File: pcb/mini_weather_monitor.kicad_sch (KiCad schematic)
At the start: 6 parts, among them U1 module_mpu6050, U2 4.0inch_SPI_MSP4021, U2_BME280 module_bme280, U3 neo6mv2, U3_BH1750 module_bh1750

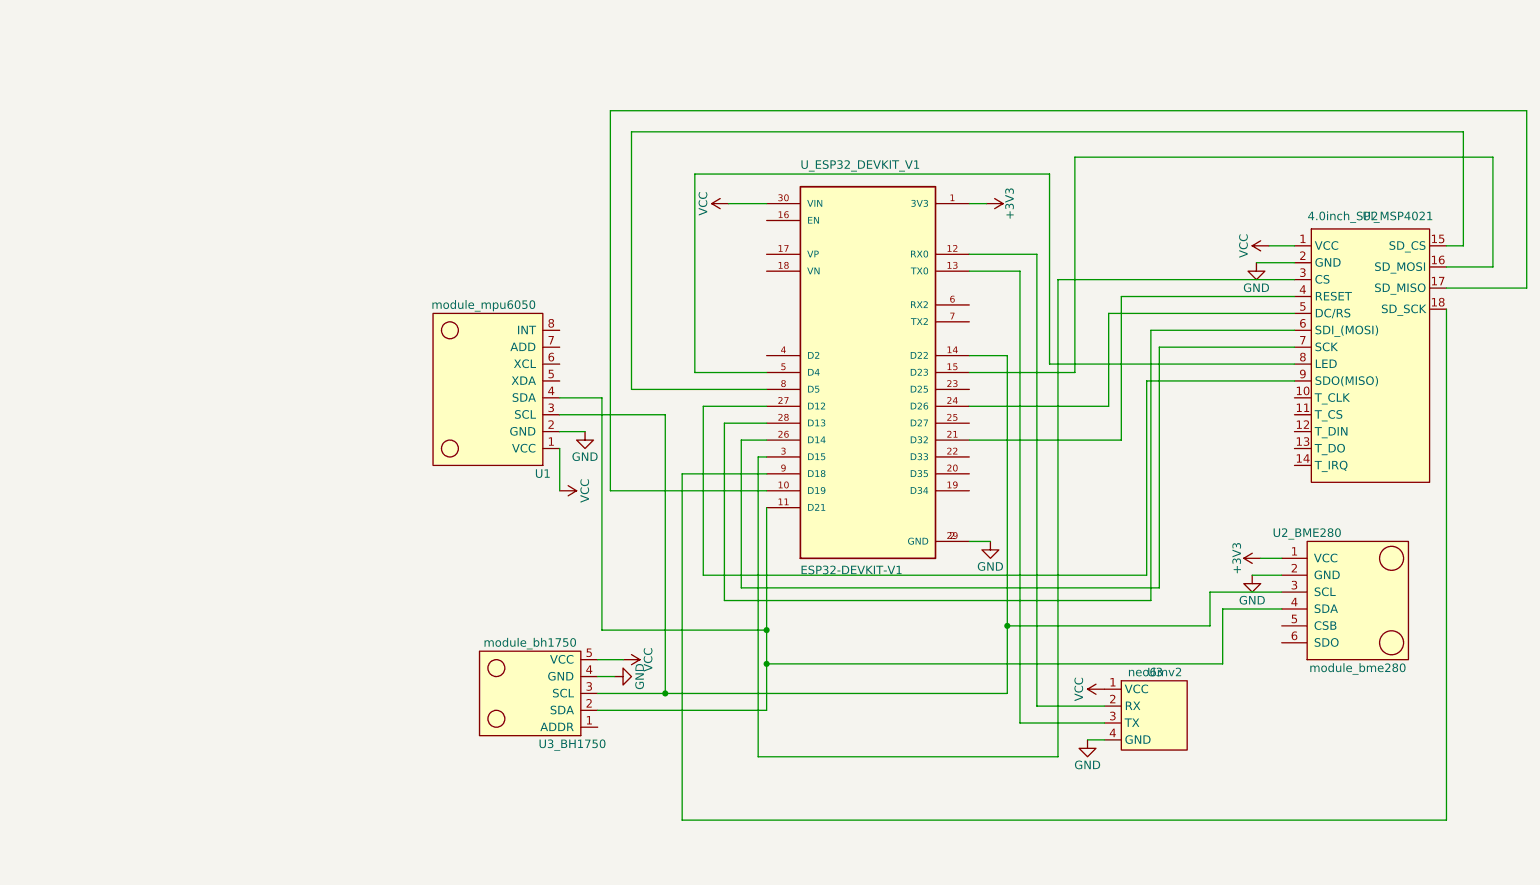
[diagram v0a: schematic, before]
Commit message: wip, with MPU6050, but will switch to SW520D
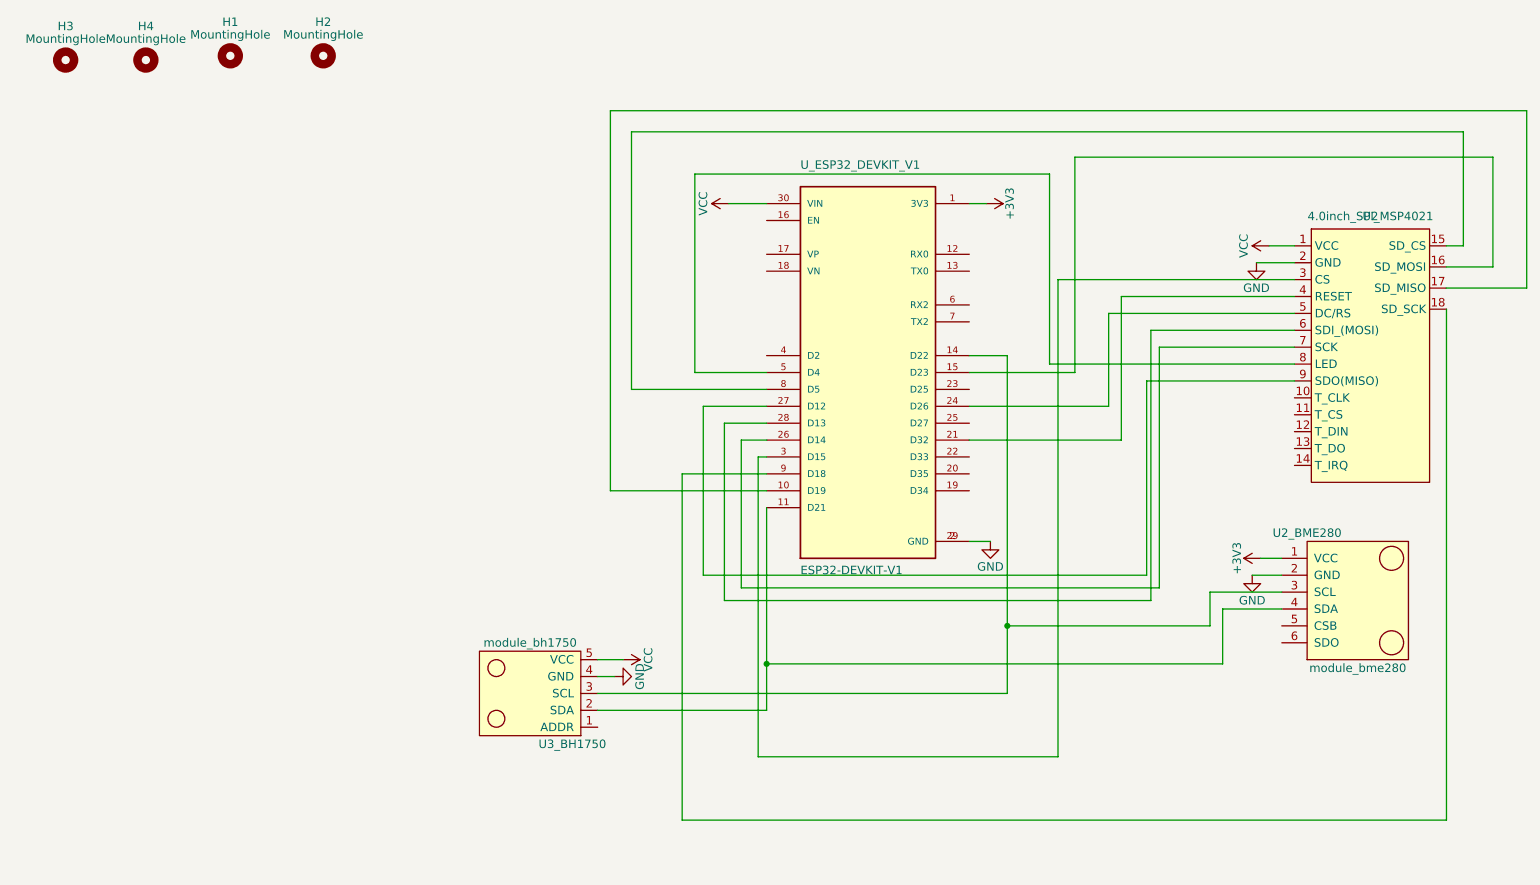
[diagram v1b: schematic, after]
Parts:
- removed U1: module_mpu6050, usini_sensors:module_mpu6050, symbol usini_sensors:module_mpu6050
- removed U3: neo6mv2, gps:GY-NEO6MV2, symbol gps:neo6mv2
- added H1, H2, H3, H4: MountingHole, MountingHole:MountingHole_2.2mm_M2, symbol Mechanical:MountingHole

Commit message: fixing orientation with new tilt sensor and adding libraries to repo
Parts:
- added J1: SW-520D, symbol Connector_Generic:Conn_01x03
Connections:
- net GND: now also J1.3 (Pin_3)
- net VCC: now also J1.2 (Pin_2)
- net at U_ESP32_DEVKIT_V1.4 (D2): now also J1.1 (Pin_1)
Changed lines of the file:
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@@
+    (stroke (width 0) (type default) (color 0 0 0 0))
+  )
+  (wire (pts (xy 78.105 86.995) (xy 98.425 86.995))
     (stroke (width 0) (type default) (color 0 0 0 0))
   )
@@
     (stroke (width 0) (type default) (color 0 0 0 0))
   )
+  (wire (pts (xy 98.425 86.995) (xy 98.425 69.215))
+    (stroke (width 0) (type default) (color 0 0 0 0))
+  )
   (wire (pts (xy 169.545 57.785) (xy 169.545 129.54))
     (stroke (width 0) (type default) (color 0 0 0 0))
@@
   )
   (wire (pts (xy 198.755 102.235) (xy 203.2 102.235))
+    (stroke (width 0) (type default) (color 0 0 0 0))
+  )
+  (wire (pts (xy 98.425 69.215) (xy 125.73 69.215))
     (stroke (width 0) (type default) (color 0 0 0 0))
   )
@@
     (pin "5")
     (pin "6")
+  )
+  (symbol (lib_id "power:VCC") (at 78.105 84.455 270) (unit 1)
+    (in_bom yes) (on_board yes)
+    (property "Reference" "#PWR?" (id 0) (at 74.295 84.455 0)
+      (effects (font (size 1.27 1.27)) hide)
+    )
+    (property "Value" "VCC" (id 1) (at 81.915 84.455 0))
+    (property "Footprint" "" (id 2) (at 78.105 84.455 0)
+      (effects (font (size 1.27 1.27)) hide)
+    )
+    (property "Datasheet" "" (id 3) (at 78.105 84.455 0)
+      (effects (font (size 1.27 1.27)) hide)
+    )
+    (pin "1")
   )
   (symbol (lib_id "Mechanical:MountingHole") (at 45.085 24.13 0) (unit 1)
@@
     (pin "1")
   )
+  (symbol (lib_id "power:GND") (at 78.105 81.915 90) (unit 1)
+    (in_bom yes) (on_board yes)
+    (property "Reference" "#PWR?" (id 0) (at 84.455 81.915 0)
+      (effects (font (size 1.27 1.27)) hide)
+    )
+    (property "Value" "GND" (id 1) (at 81.915 81.915 0))
+    (property "Footprint" "" (id 2) (at 78.105 81.915 0)
+      (effects (font (size 1.27 1.27)) hide)
+    )
+    (property "Datasheet" "" (id 3) (at 78.105 81.915 0)
+      (effects (font (size 1.27 1.27)) hide)
+    )
+    (pin "1")
+  )
   (symbol (lib_id "usini_sensors:module_bh1750") (at 100.33 117.475 180) (unit 1)
     (in_bom yes) (on_board yes)
@@
     (pin "4")
     (pin "5")
+  )
+  (symbol (lib_id "Connector_Generic:Conn_01x03") (at 73.025 84.455 180) (unit 1)
+    (in_bom yes) (on_board yes)
+    (property "Reference" "J1" (id 0) (at 73.025 89.535 0))
+    (property "Value" "SW-520D" (id 1) (at 73.025 79.375 0))
+    (property "Footprint" "" (id 2) (at 73.025 84.455 0)
+      (effects (font (size 1.27 1.27)) hide)
+    )
+    (property "Datasheet" "~" (id 3) (at 73.025 84.455 0)
+      (effects (font (size 1.27 1.27)) hide)
+    )
+    (pin "1")
+    (pin "2")
+    (pin "3")
   )
   (symbol (lib_id "power:GND") (at 199.39 55.245 0) (unit 1)
@@
       (reference "#PWR0111") (unit 1) (value "VCC") (footprint "")
     )
+    (path "/1e01b4d9-a989-409c-94fd-57d5171ccf78"
+      (reference "#PWR?") (unit 1) (value "VCC") (footprint "")
+    )
+    (path "/47b6694c-c477-4176-af38-50c331ec0ae7"
+      (reference "#PWR?") (unit 1) (value "GND") (footprint "")
+    )
     (path "/1ed3e5bb-623c-4717-afd1-5e05574edbe0"
       (reference "H1") (unit 1) (value "MountingHole") (footprint "MountingHole:MountingHole_2.2mm_M2")
@@
       (reference "H4") (unit 1) (value "MountingHole") (footprint "MountingHole:MountingHole_2.2mm_M2")
     )
+    (path "/614a403a-474a-4306-b606-97f15c564ef8"
+      (reference "J1") (unit 1) (value "SW-520D") (footprint "")
+    )
     (path "/2aa21e55-25c6-4cf4-bd8a-94f164963f6d"

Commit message: fixxing footprint and pad
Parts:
- added U1: PowerSupplyMB102_v13, power_supplies:POWERSUPPLYMB102, symbol power_supplyies:PowerSupplyMB102_v13
- J1: footprint (none) -> Connector_PinHeader_2.54mm:PinHeader_1x03_P2.54mm_Horizontal
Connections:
- net +3V3: now also U1.5 (VCC2), U1.7 (VCC2)
- net GND: now also U1.2 (GND), U1.6 (GND), U1.8 (GND)
- net VCC: now also U1.1 (VCC1), U1.3 (VCC1)
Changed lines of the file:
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@@
   (symbol (lib_id "power:VCC") (at 78.105 84.455 270) (unit 1)
     (in_bom yes) (on_board yes)
-    (property "Reference" "#PWR?" (id 0) (at 74.295 84.455 0)
+    (property "Reference" "#PWR0102" (id 0) (at 74.295 84.455 0)
       (effects (font (size 1.27 1.27)) hide)
     )
@@
     )
     (property "Datasheet" "" (id 3) (at 159.385 97.155 0)
+      (effects (font (size 1.27 1.27)) hide)
+    )
+    (pin "1")
+  )
+  (symbol (lib_id "power:VCC") (at 82.55 38.1 270) (unit 1)
+    (in_bom yes) (on_board yes)
+    (property "Reference" "#PWR0114" (id 0) (at 78.74 38.1 0)
+      (effects (font (size 1.27 1.27)) hide)
+    )
+    (property "Value" "VCC" (id 1) (at 86.36 38.1 0))
+    (property "Footprint" "" (id 2) (at 82.55 38.1 0)
+      (effects (font (size 1.27 1.27)) hide)
+    )
+    (property "Datasheet" "" (id 3) (at 82.55 38.1 0)
       (effects (font (size 1.27 1.27)) hide)
     )
@@
   (symbol (lib_id "power:GND") (at 78.105 81.915 90) (unit 1)
     (in_bom yes) (on_board yes)
-    (property "Reference" "#PWR?" (id 0) (at 84.455 81.915 0)
+    (property "Reference" "#PWR0105" (id 0) (at 84.455 81.915 0)
       (effects (font (size 1.27 1.27)) hide)
     )
@@
     )
     (property "Datasheet" "" (id 3) (at 78.105 81.915 0)
+      (effects (font (size 1.27 1.27)) hide)
+    )
+    (pin "1")
+  )
+  (symbol (lib_id "power:+3V3") (at 21.59 38.1 90) (unit 1)
+    (in_bom yes) (on_board yes)
+    (property "Reference" "#PWR0112" (id 0) (at 25.4 38.1 0)
+      (effects (font (size 1.27 1.27)) hide)
+    )
+    (property "Value" "+3V3" (id 1) (at 18.034 38.1 0))
+    (property "Footprint" "" (id 2) (at 21.59 38.1 0)
+      (effects (font (size 1.27 1.27)) hide)
+    )
+    (property "Datasheet" "" (id 3) (at 21.59 38.1 0)
       (effects (font (size 1.27 1.27)) hide)
     )
@@
     (property "Reference" "J1" (id 0) (at 73.025 89.535 0))
     (property "Value" "SW-520D" (id 1) (at 73.025 79.375 0))
-    (property "Footprint" "" (id 2) (at 73.025 84.455 0)
+    (property "Footprint" "Connector_PinHeader_2.54mm:PinHeader_1x03_P2.54mm_Horizontal" (id 2) (at 73.025 84.455 0)
       (effects (font (size 1.27 1.27)) hide)
     )
@@
     )
     (property "Datasheet" "" (id 3) (at 199.39 55.245 0)
+      (effects (font (size 1.27 1.27)) hide)
+    )
+    (pin "1")
+  )
+  (symbol (lib_id "power:GND") (at 82.55 42.418 0) (unit 1)
+    (in_bom yes) (on_board yes)
+    (property "Reference" "#PWR0117" (id 0) (at 82.55 48.768 0)
+      (effects (font (size 1.27 1.27)) hide)
+    )
+    (property "Value" "GND" (id 1) (at 82.55 46.228 0))
+    (property "Footprint" "" (id 2) (at 82.55 42.418 0)
+      (effects (font (size 1.27 1.27)) hide)
+    )
+    (property "Datasheet" "" (id 3) (at 82.55 42.418 0)
       (effects (font (size 1.27 1.27)) hide)
     )
@@
     )
     (property "Datasheet" "" (id 3) (at 201.295 52.705 0)
+      (effects (font (size 1.27 1.27)) hide)
+    )
+    (pin "1")
+  )
+  (symbol (lib_id "power:GND") (at 82.55 59.055 0) (unit 1)
+    (in_bom yes) (on_board yes)
+    (property "Reference" "#PWR0119" (id 0) (at 82.55 65.405 0)
+      (effects (font (size 1.27 1.27)) hide)
+    )
+    (property "Value" "GND" (id 1) (at 82.55 62.865 0))
+    (property "Footprint" "" (id 2) (at 82.55 59.055 0)
+      (effects (font (size 1.27 1.27)) hide)
+    )
+    (property "Datasheet" "" (id 3) (at 82.55 59.055 0)
       (effects (font (size 1.27 1.27)) hide)
     )
@@
     (pin "9")
   )
+  (symbol (lib_id "power:GND") (at 21.59 58.674 0) (unit 1)
+    (in_bom yes) (on_board yes)
+    (property "Reference" "#PWR0116" (id 0) (at 21.59 65.024 0)
+      (effects (font (size 1.27 1.27)) hide)
+    )
+    (property "Value" "GND" (id 1) (at 21.59 62.484 0))
+    (property "Footprint" "" (id 2) (at 21.59 58.674 0)
+      (effects (font (size 1.27 1.27)) hide)
+    )
+    (property "Datasheet" "" (id 3) (at 21.59 58.674 0)
+      (effects (font (size 1.27 1.27)) hide)
+    )
+    (pin "1")
+  )
   (symbol (lib_id "power:+3V3") (at 200.025 99.695 90) (unit 1)
     (in_bom yes) (on_board yes)
@@
     )
   )
+  (symbol (lib_id "power_supplyies:PowerSupplyMB102_v13") (at 52.07 48.26 0) (unit 1)
+    (in_bom yes) (on_board yes)
+    (property "Reference" "U1" (id 0) (at 52.07 46.99 0))
+    (property "Value" "PowerSupplyMB102_v13" (id 1) (at 52.07 49.53 0))
+    (property "Footprint" "power_supplies:POWERSUPPLYMB102" (id 2) (at 52.07 48.26 0)
+      (effects (font (size 1.27 1.27)) hide)
+    )
+    (property "Datasheet" "" (id 3) (at 52.07 48.26 0)
+      (effects (font (size 1.27 1.27)) hide)
+    )
+    (pin "1")
+    (pin "2")
+    (pin "3")
+    (pin "4")
+    (pin "5")
+    (pin "6")
+    (pin "7")
+    (pin "8")
+  )
+  (symbol (lib_id "power:VCC") (at 82.55 54.61 270) (unit 1)
+    (in_bom yes) (on_board yes)
+    (property "Reference" "#PWR0118" (id 0) (at 78.74 54.61 0)
+      (effects (font (size 1.27 1.27)) hide)
+    )
+    (property "Value" "VCC" (id 1) (at 86.36 54.61 0))
+    (property "Footprint" "" (id 2) (at 82.55 54.61 0)
+      (effects (font (size 1.27 1.27)) hide)
+    )
+    (property "Datasheet" "" (id 3) (at 82.55 54.61 0)
+      (effects (font (size 1.27 1.27)) hide)
+    )
+    (pin "1")
+  )
   (symbol (lib_id "power:VCC") (at 104.14 114.935 270) (unit 1)
     (in_bom yes) (on_board yes)
@@
     )
   )
+  (symbol (lib_id "power:GND") (at 21.59 42.418 0) (unit 1)
+    (in_bom yes) (on_board yes)
+    (property "Reference" "#PWR0115" (id 0) (at 21.59 48.768 0)
+      (effects (font (size 1.27 1.27)) hide)
+    )
+    (property "Value" "GND" (id 1) (at 21.59 46.228 0))
+    (property "Footprint" "" (id 2) (at 21.59 42.418 0)
+      (effects (font (size 1.27 1.27)) hide)
+    )
+    (property "Datasheet" "" (id 3) (at 21.59 42.418 0)
+      (effects (font (size 1.27 1.27)) hide)
+    )
+    (pin "1")
+  )
   (symbol (lib_id "power:VCC") (at 120.015 46.355 90) (unit 1)
     (in_bom yes) (on_board yes)
@@
     )
     (property "Datasheet" "" (id 3) (at 120.015 46.355 0)
+      (effects (font (size 1.27 1.27)) hide)
+    )
+    (pin "1")
+  )
+  (symbol (lib_id "power:+3V3") (at 21.59 54.356 90) (unit 1)
+    (in_bom yes) (on_board yes)
+    (property "Reference" "#PWR0113" (id 0) (at 25.4 54.356 0)
+      (effects (font (size 1.27 1.27)) hide)
+    )
+    (property "Value" "+3V3" (id 1) (at 18.034 54.356 0))
+    (property "Footprint" "" (id 2) (at 21.59 54.356 0)
+      (effects (font (size 1.27 1.27)) hide)
+    )
+    (property "Datasheet" "" (id 3) (at 21.59 54.356 0)
       (effects (font (size 1.27 1.27)) hide)
     )
@@
       (reference "#PWR0101") (unit 1) (value "GND") (footprint "")
     )
+    (path "/1e01b4d9-a989-409c-94fd-57d5171ccf78"
+      (reference "#PWR0102") (unit 1) (value "VCC") (footprint "")
+    )
     (path "/1f388e68-7a67-4769-ab0f-bc8bbfd33e19"
       (reference "#PWR0103") (unit 1) (value "GND") (footprint "")
@@
       (reference "#PWR0104") (unit 1) (value "GND") (footprint "")
     )
+    (path "/47b6694c-c477-4176-af38-50c331ec0ae7"
+      (reference "#PWR0105") (unit 1) (value "GND") (footprint "")
+    )
     (path "/3db7a179-de3e-48c9-994f-6f4a8f7a50e2"
       (reference "#PWR0106") (unit 1) (value "+3V3") (footprint "")
@@
       (reference "#PWR0111") (unit 1) (value "VCC") (footprint "")
     )
-    (path "/1e01b4d9-a989-409c-94fd-57d5171ccf78"
-      (reference "#PWR?") (unit 1) (value "VCC") (footprint "")
-    )
-    (path "/47b6694c-c477-4176-af38-50c331ec0ae7"
-      (reference "#PWR?") (unit 1) (value "GND") (footprint "")
+    (path "/4f3560be-1f70-4fa1-aade-f6678352e498"
+      (reference "#PWR0112") (unit 1) (value "+3V3") (footprint "")
+    )
+    (path "/fa6e591d-2fb3-41d0-89e1-7ff8a72bbcbf"
+      (reference "#PWR0113") (unit 1) (value "+3V3") (footprint "")
+    )
+    (path "/26ee0bb2-ad6d-413d-98eb-7ee5ee45f359"
+      (reference "#PWR0114") (unit 1) (value "VCC") (footprint "")
+    )
+    (path "/f2ef21bc-1542-49c2-acb2-773f89f4450e"
+      (reference "#PWR0115") (unit 1) (value "GND") (footprint "")
+    )
+    (path "/b5d4c2a9-513a-4b02-8fe0-a6fb67e94f7f"
+      (reference "#PWR0116") (unit 1) (value "GND") (footprint "")
+    )
+    (path "/6ee1587a-a7da-4728-ab8c-6e3d2518a1e3"
+      (reference "#PWR0117") (unit 1) (value "GND") (footprint "")
+    )
+    (path "/dd7408e6-f877-4a6b-998a-3f52cade8029"
+      (reference "#PWR0118") (unit 1) (value "VCC") (footprint "")
+    )
+    (path "/a77e472e-db3b-404f-8e27-ca00131b5c5a"
+      (reference "#PWR0119") (unit 1) (value "GND") (footprint "")
     )
     (path "/1ed3e5bb-623c-4717-afd1-5e05574edbe0"
@@
     )
     (path "/614a403a-474a-4306-b606-97f15c564ef8"
-      (reference "J1") (unit 1) (value "SW-520D") (footprint "")
+      (reference "J1") (unit 1) (value "SW-520D") (footprint "Connector_PinHeader_2.54mm:PinHeader_1x03_P2.54mm_Horizontal")
+    )
+    (path "/d768292d-7ad8-48cb-973b-82d3c96ed0e4"
+      (reference "U1") (unit 1) (value "PowerSupplyMB102_v13") (footprint "power_supplies:POWERSUPPLYMB102")
     )
     (path "/2aa21e55-25c6-4cf4-bd8a-94f164963f6d"

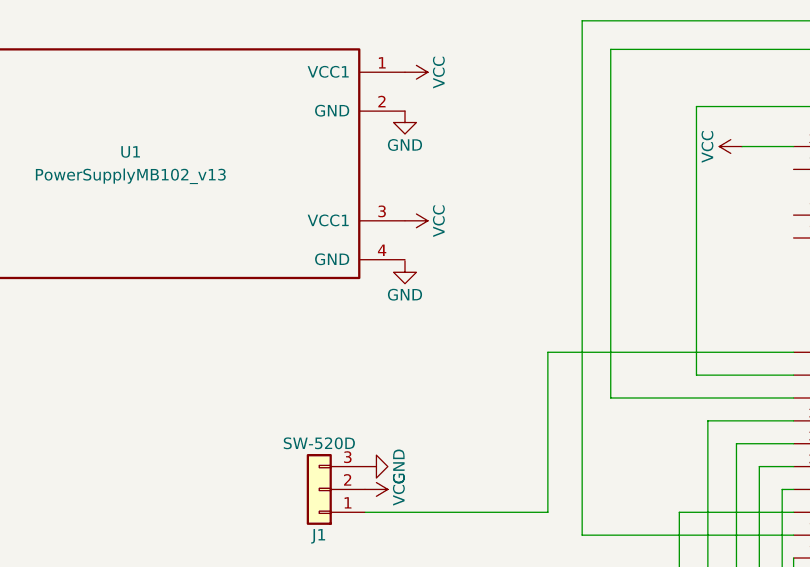
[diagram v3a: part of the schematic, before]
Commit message: trace cleanup
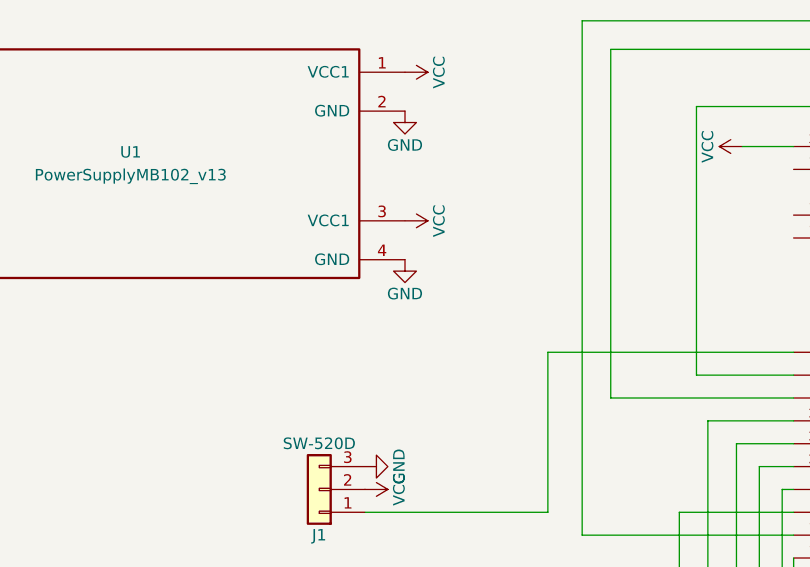
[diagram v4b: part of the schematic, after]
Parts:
- J1: footprint Connector_PinHeader_2.54mm:PinHeader_1x03_P2.54mm_Horizontal -> tilt:KY020 Tilt
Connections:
- net GND: now also U1.4 (GND)
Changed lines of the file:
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@@
     (property "Reference" "J1" (id 0) (at 73.025 89.535 0))
     (property "Value" "SW-520D" (id 1) (at 73.025 79.375 0))
-    (property "Footprint" "Connector_PinHeader_2.54mm:PinHeader_1x03_P2.54mm_Horizontal" (id 2) (at 73.025 84.455 0)
+    (property "Footprint" "tilt:KY020 Tilt" (id 2) (at 73.025 84.455 0)
       (effects (font (size 1.27 1.27)) hide)
     )
@@
     (pin "1")
   )
-  (symbol (lib_id "power:GND") (at 82.55 59.055 0) (unit 1)
-    (in_bom yes) (on_board yes)
-    (property "Reference" "#PWR0119" (id 0) (at 82.55 65.405 0)
-      (effects (font (size 1.27 1.27)) hide)
-    )
-    (property "Value" "GND" (id 1) (at 82.55 62.865 0))
-    (property "Footprint" "" (id 2) (at 82.55 59.055 0)
-      (effects (font (size 1.27 1.27)) hide)
-    )
-    (property "Datasheet" "" (id 3) (at 82.55 59.055 0)
+  (symbol (lib_id "power:GND") (at 82.55 58.928 0) (unit 1)
+    (in_bom yes) (on_board yes)
+    (property "Reference" "#PWR0119" (id 0) (at 82.55 65.278 0)
+      (effects (font (size 1.27 1.27)) hide)
+    )
+    (property "Value" "GND" (id 1) (at 82.55 62.738 0))
+    (property "Footprint" "" (id 2) (at 82.55 58.928 0)
+      (effects (font (size 1.27 1.27)) hide)
+    )
+    (property "Datasheet" "" (id 3) (at 82.55 58.928 0)
       (effects (font (size 1.27 1.27)) hide)
     )
@@
     )
     (path "/614a403a-474a-4306-b606-97f15c564ef8"
-      (reference "J1") (unit 1) (value "SW-520D") (footprint "Connector_PinHeader_2.54mm:PinHeader_1x03_P2.54mm_Horizontal")
+      (reference "J1") (unit 1) (value "SW-520D") (footprint "tilt:KY020 Tilt")
     )
     (path "/d768292d-7ad8-48cb-973b-82d3c96ed0e4"
